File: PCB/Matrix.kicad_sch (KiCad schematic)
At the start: 109 parts, among them SW1 Bootsel, SW1 CPG151101S11, SW10 CPG151101S11, SW11 CPG151101S11, SW12 CPG151101S11, SW13 CPG151101S11, SW14 CPG151101S11, SW15 CPG151101S11, SW16 CPG151101S11, SW17 CPG151101S11, SW18 CPG151101S11, SW19 CPG151101S11, SW2 CPG151101S11, SW20 CPG151101S11, SW21 CPG151101S11, SW22 CPG151101S11, SW23 CPG151101S11, SW24 CPG151101S11, SW25 CPG151101S11, SW26 CPG151101S11, SW27 CPG151101S11, SW28 CPG151101S11, SW29 CPG151101S11, SW3 CPG151101S11, SW30 CPG151101S11, SW31 CPG151101S11, SW32 CPG151101S11, SW33 CPG151101S11, SW34 CPG151101S11, SW35 CPG151101S11, SW36 CPG151101S11, SW37 CPG151101S11, SW38 CPG151101S11, SW39 CPG151101S11, SW4 CPG151101S11, SW40 CPG151101S11, SW41 CPG151101S11, SW42 CPG151101S11, SW43 CPG151101S11, SW44 CPG151101S11, SW45 CPG151101S11, SW46 CPG151101S11, SW47 CPG151101S11, SW48 CPG151101S11, SW49 CPG151101S11, SW5 CPG151101S11, SW50 CPG151101S11, SW51 CPG151101S11, SW52 CPG151101S11, SW53 CPG151101S11, SW54 CPG151101S11, SW55 CPG151101S11, SW56 CPG151101S11, SW57 CPG151101S11, SW58 CPG151101S11, SW59 CPG151101S11, SW6 CPG151101S11, SW60 CPG151101S11, SW61 CPG151101S11, SW62 CPG151101S11, SW63 CPG151101S11, SW64 CPG151101S11, SW66 EC10E, SW7 CPG151101S11, SW8 CPG151101S11, SW9 CPG151101S11, U6 74HC595, U7 74HC595

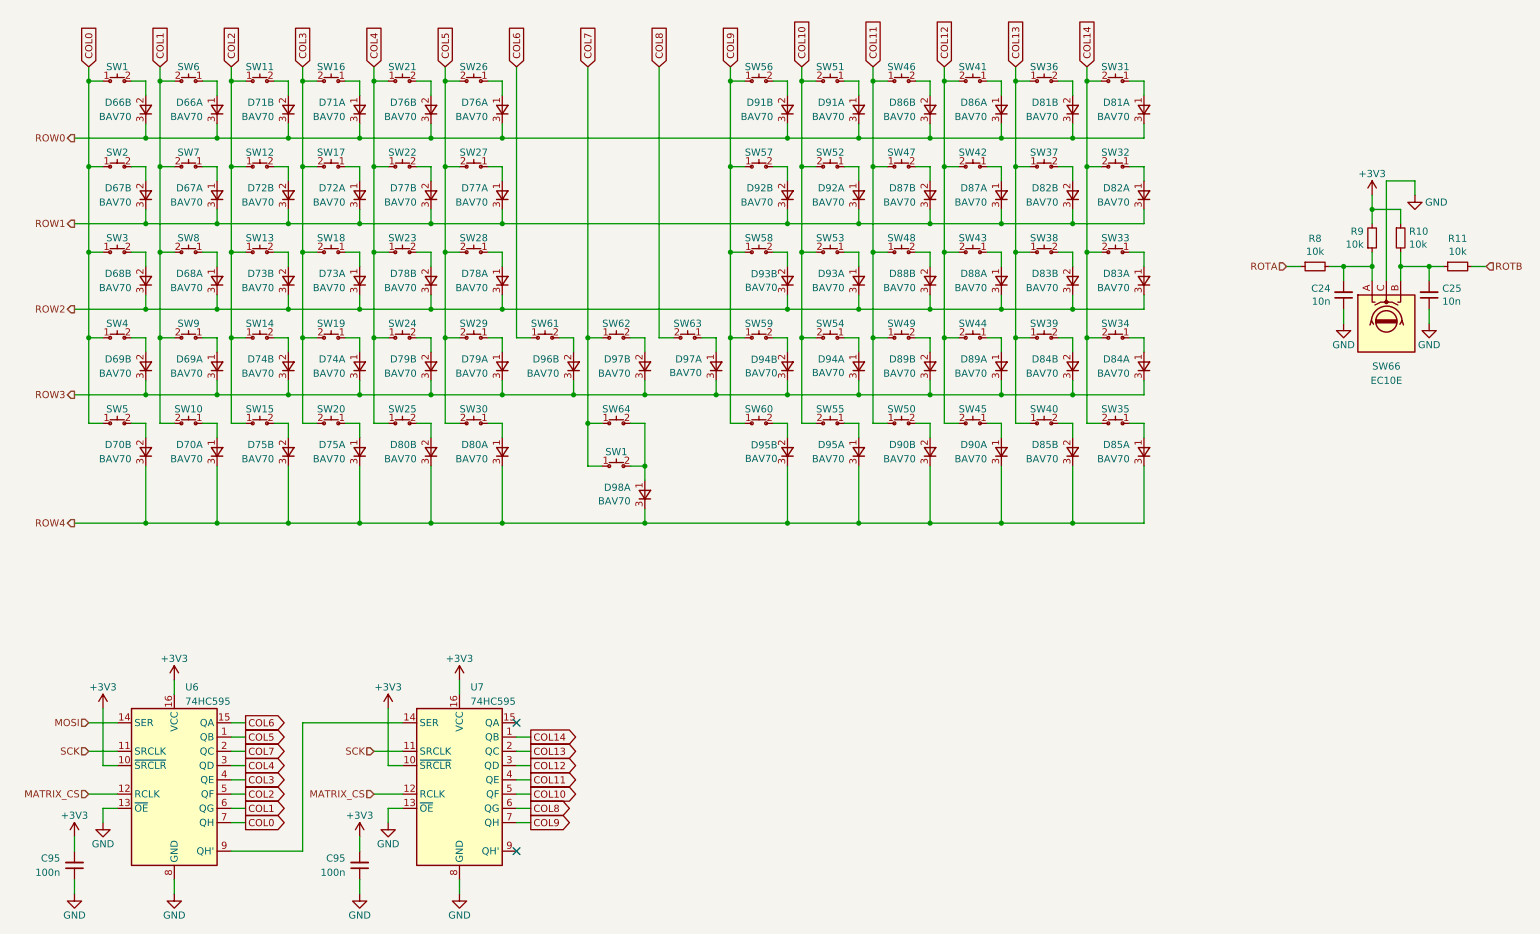
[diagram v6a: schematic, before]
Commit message: 27/08/2023 update
Added unified library for all symbols, footprints and 3D files. Changed MCU to STM32F072RBT6. Removed OLED, voltage and current sensing, USB CC circuitry and shift registers. Changed ESD protection chip. Cleaned up routing and component placement. Changed SWD header pinout to 6-pin standard.
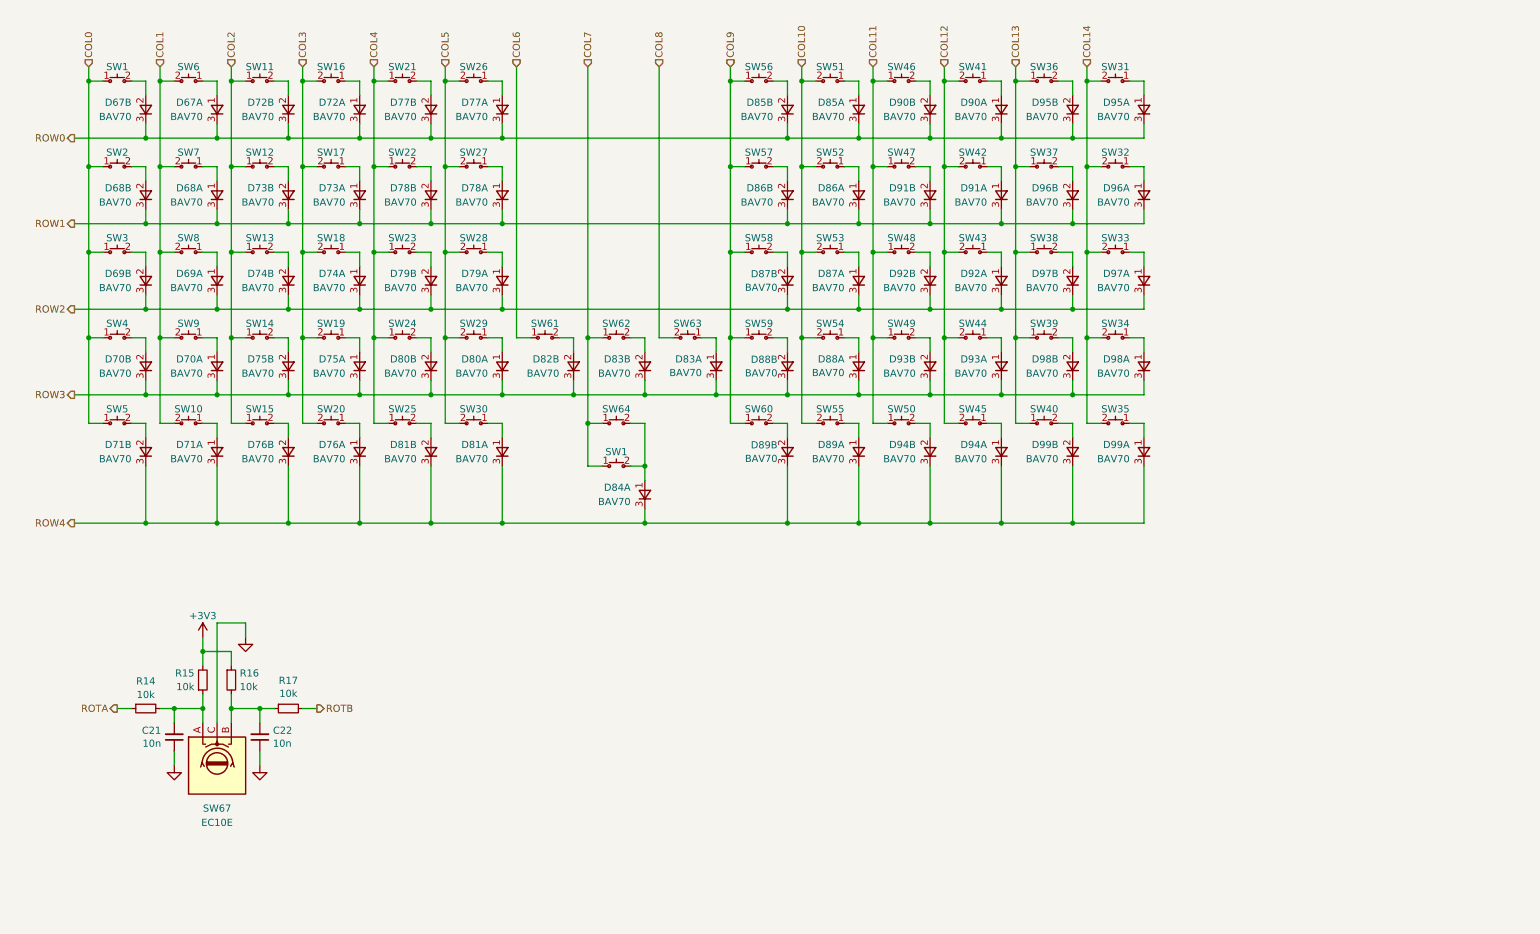
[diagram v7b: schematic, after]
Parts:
- removed C95 (x2): 100n, Capacitor_SMD:C_0402_1005Metric, symbol Device:C_Small
- removed D98: BAV70, Honeydew:SOT-23-3, symbol Honeydew:D_Dual_CommonCathode_AAK_Split_Small
- removed U6, U7: 74HC595, Honeydew:SOIC-16_3.9x9.9mm_P1.27mm, symbol 74xx:74HC595
- added D84: BAV70, Ariamelon-Package:SOT-23-3, symbol Ariamelon-Device:D_Dual_CommonCathode_AAK_Split_Small
- C21: renamed from C24; footprint Capacitor_SMD:C_0402_1005Metric -> Ariamelon-Device:C_0402_1005Metric
- C22: renamed from C25; footprint Capacitor_SMD:C_0402_1005Metric -> Ariamelon-Device:C_0402_1005Metric
- D67: renamed from D66; footprint Honeydew:SOT-23-3 -> Ariamelon-Package:SOT-23-3; symbol Honeydew:D_Dual_CommonCathode_AAK_Split_Small -> Ariamelon-Device:D_Dual_CommonCathode_AAK_Split_Small
- D68: renamed from D67; footprint Honeydew:SOT-23-3 -> Ariamelon-Package:SOT-23-3; symbol Honeydew:D_Dual_CommonCathode_AAK_Split_Small -> Ariamelon-Device:D_Dual_CommonCathode_AAK_Split_Small
- D69: renamed from D68; footprint Honeydew:SOT-23-3 -> Ariamelon-Package:SOT-23-3; symbol Honeydew:D_Dual_CommonCathode_AAK_Split_Small -> Ariamelon-Device:D_Dual_CommonCathode_AAK_Split_Small
- D70: renamed from D69; footprint Honeydew:SOT-23-3 -> Ariamelon-Package:SOT-23-3; symbol Honeydew:D_Dual_CommonCathode_AAK_Split_Small -> Ariamelon-Device:D_Dual_CommonCathode_AAK_Split_Small
- D71: renamed from D70; footprint Honeydew:SOT-23-3 -> Ariamelon-Package:SOT-23-3; symbol Honeydew:D_Dual_CommonCathode_AAK_Split_Small -> Ariamelon-Device:D_Dual_CommonCathode_AAK_Split_Small
- D72: renamed from D71; footprint Honeydew:SOT-23-3 -> Ariamelon-Package:SOT-23-3; symbol Honeydew:D_Dual_CommonCathode_AAK_Split_Small -> Ariamelon-Device:D_Dual_CommonCathode_AAK_Split_Small
- D73: renamed from D72; footprint Honeydew:SOT-23-3 -> Ariamelon-Package:SOT-23-3; symbol Honeydew:D_Dual_CommonCathode_AAK_Split_Small -> Ariamelon-Device:D_Dual_CommonCathode_AAK_Split_Small
- D74: renamed from D73; footprint Honeydew:SOT-23-3 -> Ariamelon-Package:SOT-23-3; symbol Honeydew:D_Dual_CommonCathode_AAK_Split_Small -> Ariamelon-Device:D_Dual_CommonCathode_AAK_Split_Small
- D75: renamed from D74; footprint Honeydew:SOT-23-3 -> Ariamelon-Package:SOT-23-3; symbol Honeydew:D_Dual_CommonCathode_AAK_Split_Small -> Ariamelon-Device:D_Dual_CommonCathode_AAK_Split_Small
- D76: renamed from D75; footprint Honeydew:SOT-23-3 -> Ariamelon-Package:SOT-23-3; symbol Honeydew:D_Dual_CommonCathode_AAK_Split_Small -> Ariamelon-Device:D_Dual_CommonCathode_AAK_Split_Small
- D77: renamed from D76; footprint Honeydew:SOT-23-3 -> Ariamelon-Package:SOT-23-3; symbol Honeydew:D_Dual_CommonCathode_AAK_Split_Small -> Ariamelon-Device:D_Dual_CommonCathode_AAK_Split_Small
- D78: renamed from D77; footprint Honeydew:SOT-23-3 -> Ariamelon-Package:SOT-23-3; symbol Honeydew:D_Dual_CommonCathode_AAK_Split_Small -> Ariamelon-Device:D_Dual_CommonCathode_AAK_Split_Small
- D79: renamed from D78; footprint Honeydew:SOT-23-3 -> Ariamelon-Package:SOT-23-3; symbol Honeydew:D_Dual_CommonCathode_AAK_Split_Small -> Ariamelon-Device:D_Dual_CommonCathode_AAK_Split_Small
- D80: renamed from D79; footprint Honeydew:SOT-23-3 -> Ariamelon-Package:SOT-23-3; symbol Honeydew:D_Dual_CommonCathode_AAK_Split_Small -> Ariamelon-Device:D_Dual_CommonCathode_AAK_Split_Small
- D81: renamed from D80; footprint Honeydew:SOT-23-3 -> Ariamelon-Package:SOT-23-3; symbol Honeydew:D_Dual_CommonCathode_AAK_Split_Small -> Ariamelon-Device:D_Dual_CommonCathode_AAK_Split_Small
- D82: renamed from D96; footprint Honeydew:SOT-23-3 -> Ariamelon-Package:SOT-23-3; symbol Honeydew:D_Dual_CommonCathode_AAK_Split_Small -> Ariamelon-Device:D_Dual_CommonCathode_AAK_Split_Small
- D83: renamed from D97; footprint Honeydew:SOT-23-3 -> Ariamelon-Package:SOT-23-3; symbol Honeydew:D_Dual_CommonCathode_AAK_Split_Small -> Ariamelon-Device:D_Dual_CommonCathode_AAK_Split_Small
- D85: renamed from D91; footprint Honeydew:SOT-23-3 -> Ariamelon-Package:SOT-23-3; symbol Honeydew:D_Dual_CommonCathode_AAK_Split_Small -> Ariamelon-Device:D_Dual_CommonCathode_AAK_Split_Small
- D86: renamed from D92; footprint Honeydew:SOT-23-3 -> Ariamelon-Package:SOT-23-3; symbol Honeydew:D_Dual_CommonCathode_AAK_Split_Small -> Ariamelon-Device:D_Dual_CommonCathode_AAK_Split_Small
- D87: renamed from D93; footprint Honeydew:SOT-23-3 -> Ariamelon-Package:SOT-23-3; symbol Honeydew:D_Dual_CommonCathode_AAK_Split_Small -> Ariamelon-Device:D_Dual_CommonCathode_AAK_Split_Small
- D88: renamed from D94; footprint Honeydew:SOT-23-3 -> Ariamelon-Package:SOT-23-3; symbol Honeydew:D_Dual_CommonCathode_AAK_Split_Small -> Ariamelon-Device:D_Dual_CommonCathode_AAK_Split_Small
- D89: renamed from D95; footprint Honeydew:SOT-23-3 -> Ariamelon-Package:SOT-23-3; symbol Honeydew:D_Dual_CommonCathode_AAK_Split_Small -> Ariamelon-Device:D_Dual_CommonCathode_AAK_Split_Small
- D90: renamed from D86; footprint Honeydew:SOT-23-3 -> Ariamelon-Package:SOT-23-3; symbol Honeydew:D_Dual_CommonCathode_AAK_Split_Small -> Ariamelon-Device:D_Dual_CommonCathode_AAK_Split_Small
- D91: renamed from D87; footprint Honeydew:SOT-23-3 -> Ariamelon-Package:SOT-23-3; symbol Honeydew:D_Dual_CommonCathode_AAK_Split_Small -> Ariamelon-Device:D_Dual_CommonCathode_AAK_Split_Small
- D92: renamed from D88; footprint Honeydew:SOT-23-3 -> Ariamelon-Package:SOT-23-3; symbol Honeydew:D_Dual_CommonCathode_AAK_Split_Small -> Ariamelon-Device:D_Dual_CommonCathode_AAK_Split_Small
- D93: renamed from D89; footprint Honeydew:SOT-23-3 -> Ariamelon-Package:SOT-23-3; symbol Honeydew:D_Dual_CommonCathode_AAK_Split_Small -> Ariamelon-Device:D_Dual_CommonCathode_AAK_Split_Small
- D94: renamed from D90; footprint Honeydew:SOT-23-3 -> Ariamelon-Package:SOT-23-3; symbol Honeydew:D_Dual_CommonCathode_AAK_Split_Small -> Ariamelon-Device:D_Dual_CommonCathode_AAK_Split_Small
- D95: renamed from D81; footprint Honeydew:SOT-23-3 -> Ariamelon-Package:SOT-23-3; symbol Honeydew:D_Dual_CommonCathode_AAK_Split_Small -> Ariamelon-Device:D_Dual_CommonCathode_AAK_Split_Small
- D96: renamed from D82; footprint Honeydew:SOT-23-3 -> Ariamelon-Package:SOT-23-3; symbol Honeydew:D_Dual_CommonCathode_AAK_Split_Small -> Ariamelon-Device:D_Dual_CommonCathode_AAK_Split_Small
- D97: renamed from D83; footprint Honeydew:SOT-23-3 -> Ariamelon-Package:SOT-23-3; symbol Honeydew:D_Dual_CommonCathode_AAK_Split_Small -> Ariamelon-Device:D_Dual_CommonCathode_AAK_Split_Small
- D98: renamed from D84; footprint Honeydew:SOT-23-3 -> Ariamelon-Package:SOT-23-3; symbol Honeydew:D_Dual_CommonCathode_AAK_Split_Small -> Ariamelon-Device:D_Dual_CommonCathode_AAK_Split_Small
- D99: renamed from D85; footprint Honeydew:SOT-23-3 -> Ariamelon-Package:SOT-23-3; symbol Honeydew:D_Dual_CommonCathode_AAK_Split_Small -> Ariamelon-Device:D_Dual_CommonCathode_AAK_Split_Small
- R14: renamed from R8; footprint Resistor_SMD:R_0402_1005Metric -> Ariamelon-Device:R_0402_1005Metric
- R15: renamed from R9; footprint Resistor_SMD:R_0402_1005Metric -> Ariamelon-Device:R_0402_1005Metric
- R16: renamed from R10; footprint Resistor_SMD:R_0402_1005Metric -> Ariamelon-Device:R_0402_1005Metric
- R17: renamed from R11; footprint Resistor_SMD:R_0402_1005Metric -> Ariamelon-Device:R_0402_1005Metric
- SW1, SW10, SW11, SW12, SW13, SW14, SW15, SW16, SW17, SW18, SW19, SW2, SW20, SW21, SW22, SW23, SW24, SW25, SW26, SW27, SW28, SW29, SW3, SW30, SW31, SW32, SW33, SW34, SW35, SW36, SW37, SW38, SW39, SW4, SW40, SW41, SW42, SW43, SW44, SW45, SW46, SW47, SW48, SW49, SW5, SW50, SW51, SW52, SW53, SW54, SW55, SW56, SW57, SW58, SW59, SW6, SW60, SW61, SW62, SW63, SW7, SW8, SW9: footprint Honeydew:MXOnly-1U-Hotswap -> Ariamelon-Switch:SW_MX_1U_Hotswap; symbol Honeydew:SW_SPST_Small -> Ariamelon-Switch:SW_Push_Small
- SW1: footprint Honeydew:SW_SPST_D2F_PTS645_SMT+THT -> Ariamelon-Switch:SW_D2F_PTS645_SMT+THT; symbol Honeydew:SW_SPST_Small -> Ariamelon-Switch:SW_Push_Small; now left out of the parts list
- SW64: footprint Honeydew:MXOnly-2U-Hotswap -> Ariamelon-Switch:SW_MX_2U_Hotswap; symbol Honeydew:SW_SPST_Small -> Ariamelon-Switch:SW_Push_Small
- SW67: renamed from SW66; footprint Honeydew:EC10E -> Ariamelon-RotaryEncoder:RotaryEncoder_Alps_EC10E; now left out of the parts list
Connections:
- net ROW4: now also D84.3 (K)
- net at SW1.2 (B), SW64.2 (B): now also D84.1 (A)
- no-connect marks 2 -> 0
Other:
- moved on the sheet: C21, C22, R14, R15, R16, R17, SW67

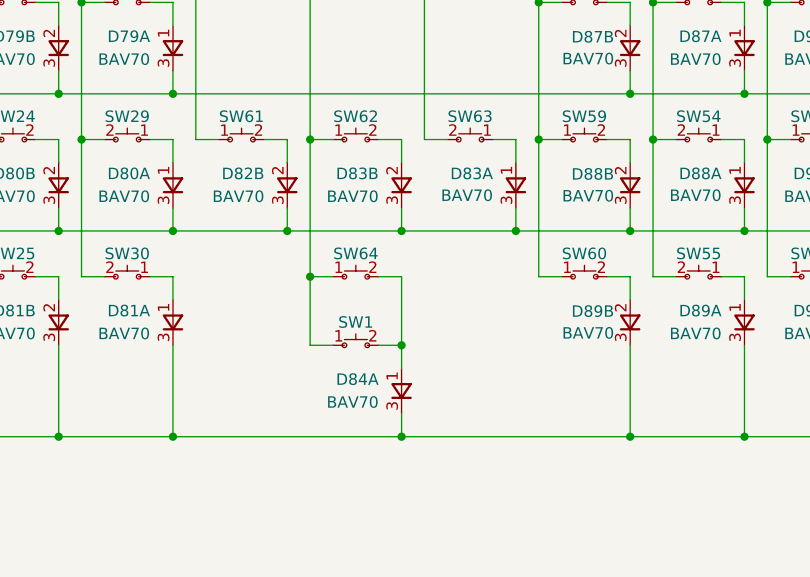
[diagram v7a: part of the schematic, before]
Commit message: 28/08/2023 update
Added test points for VIK connector. Refined case and scrollwheel design. Added pull-up resistor to RGB trace. Added Acheron single-push reset circuit. Updated STEP files.
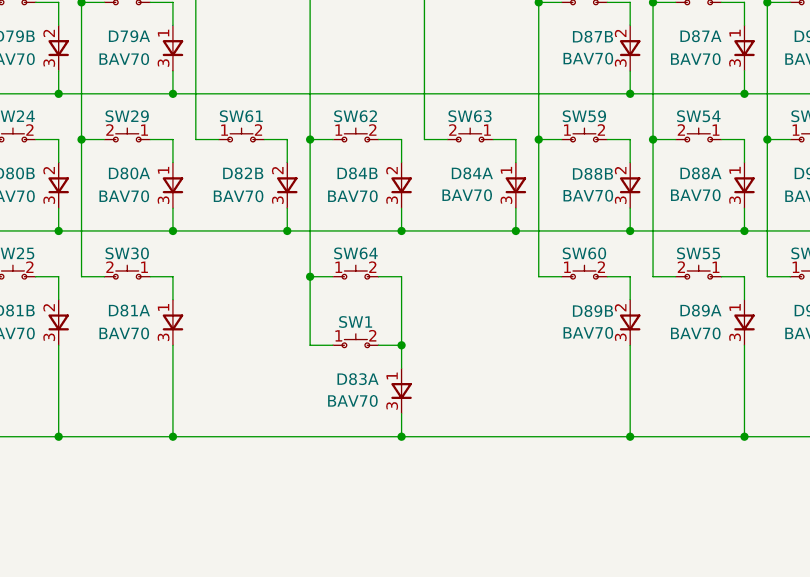
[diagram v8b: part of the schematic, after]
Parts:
- renumbered D84 to D83, D83 to D84
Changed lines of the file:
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@@
   (title_block
     (title "Honeydew unified split ergonomic keyboard")
-    (date "2023-08-27")
+    (date "2023-08-28")
     (rev "V3.0")
     (company "Created by Ariamelon (https://github.com/Ariamelon/Honeydew/)")
@@
   (symbol (lib_id "Ariamelon-Device:D_Dual_CommonCathode_AAK_Split_Small") (at 139.7 76.2 270) (unit 1)
     (in_bom yes) (on_board yes) (dnp no) (fields_autoplaced)
-    (property "Reference" "D83" (at 137.16 74.93 90)
+    (property "Reference" "D84" (at 137.16 74.93 90)
       (effects (font (size 1.27 1.27)) (justify right))
     )
@@
       (project "Honeydew"
         (path "/534caec7-cf60-4f90-b1ed-42c9d445ef0f/c1819a82-630d-421e-8b73-d65ee471609e"
-          (reference "D83") (unit 1)
+          (reference "D84") (unit 1)
         )
       )
@@
   )
   (symbol (lib_id "Ariamelon-Device:D_Dual_CommonCathode_AAK_Split_Small") (at 127 99.06 270) (unit 1)
-    (in_bom yes) (on_board yes) (dnp no) (fields_autoplaced)
-    (property "Reference" "D84" (at 124.46 97.79 90)
+    (in_bom yes) (on_board yes) (dnp no)
+    (property "Reference" "D83" (at 124.46 97.79 90)
       (effects (font (size 1.27 1.27)) (justify right))
     )
-    (property "Value" "BAV70" (at 124.46 100.33 90)
+    (property "Value" "BAV70" (at 124.46 100.2142 90)
       (effects (font (size 1.27 1.27)) (justify right))
     )
@@
       (project "Honeydew"
         (path "/534caec7-cf60-4f90-b1ed-42c9d445ef0f/c1819a82-630d-421e-8b73-d65ee471609e"
-          (reference "D84") (unit 1)
+          (reference "D83") (unit 1)
         )
       )
@@
   (symbol (lib_id "Ariamelon-Device:D_Dual_CommonCathode_AAK_Split_Small") (at 127 76.2 270) (unit 2)
     (in_bom yes) (on_board yes) (dnp no) (fields_autoplaced)
-    (property "Reference" "D83" (at 124.46 74.93 90)
+    (property "Reference" "D84" (at 124.46 74.93 90)
       (effects (font (size 1.27 1.27)) (justify right))
     )
@@
       (project "Honeydew"
         (path "/534caec7-cf60-4f90-b1ed-42c9d445ef0f/c1819a82-630d-421e-8b73-d65ee471609e"
-          (reference "D83") (unit 2)
+          (reference "D84") (unit 2)
         )
       )
